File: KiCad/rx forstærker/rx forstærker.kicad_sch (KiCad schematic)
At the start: 11 parts, among them U1 MCP6002-xMC

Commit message: Rx forstærker uden kond
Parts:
- removed C_elektrolyt: 10uF, symbol Device:C
- removed C_evt_elekt+keram: C_Find_værdi, symbol Device:C
- removed C_keramisk: 100nF, symbol Device:C
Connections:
- net VS: now also R1,3.2, U1.3 (+)
- net at R1,1.1, R1,2.1, R1,3.1: now also R3.1, R4.2
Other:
- moved on the sheet: R3, R4

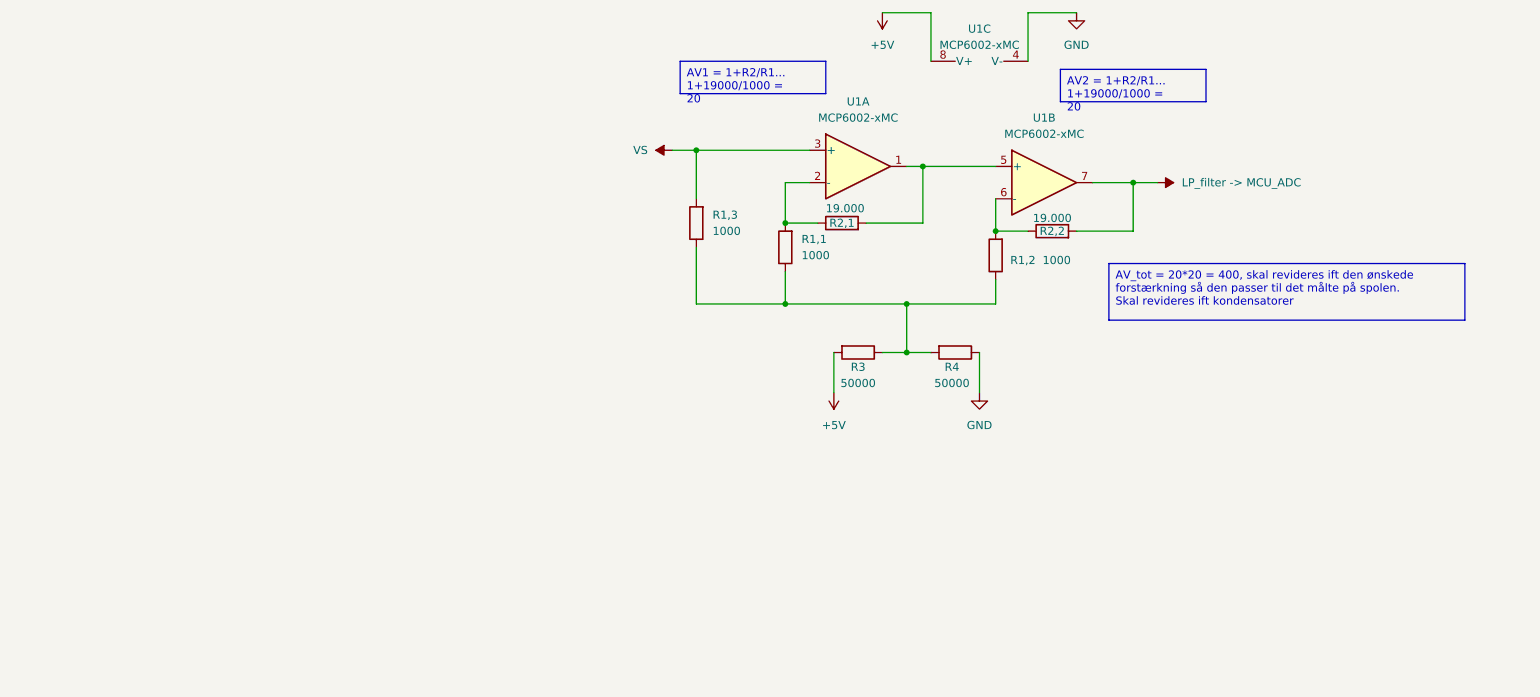
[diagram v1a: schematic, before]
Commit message: RX forstærker + MCU i kicad,mangler footprints2
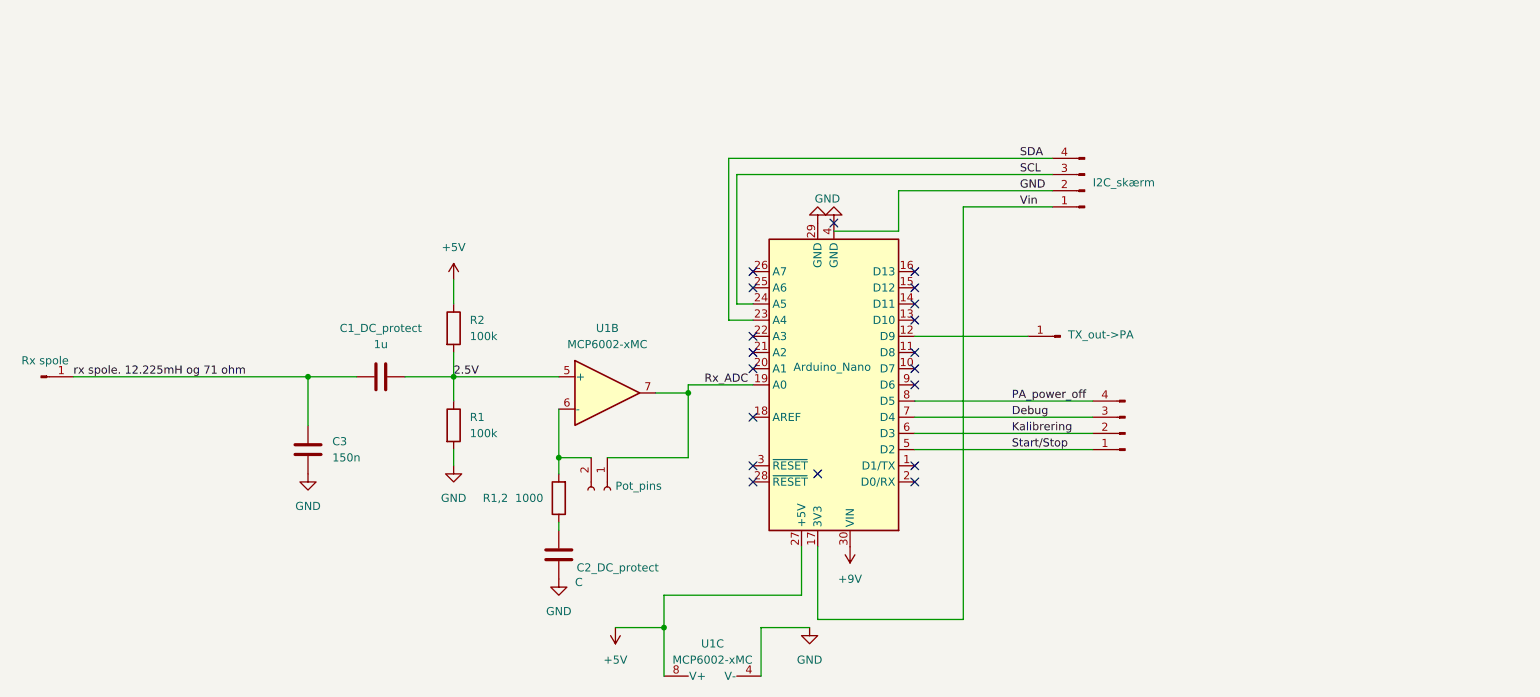
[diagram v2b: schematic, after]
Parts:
- removed R1,1, R1,3: 1000, symbol Device:R
- removed R2,1, R2,2: 19.000, symbol Device:R
- removed R3, R4: 50000, symbol Device:R
- removed unit 1 of U1
- added A1: Arduino_Nano, Module:Arduino_Nano, symbol MCU_Module:Arduino_Nano_v3.x
- added C1_DC_protect: 1u, symbol Device:C
- added C2_DC_protect: C, symbol Device:C
- added C3: 150n, symbol Device:C
- added I2C_skærm, J4: Conn_01x04_Pin, symbol Connector:Conn_01x04_Pin
- added J1: Rx spole, symbol Connector:Conn_01x01_Pin
- added J2: Pot_pins, symbol Connector:Conn_01x02_Socket
- added J3: TX_out->PA, symbol Connector:Conn_01x01_Pin
- added R1, R2: 100k, symbol Device:R
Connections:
- net +5V: now also A1.27 (+5V), R2.1
- net GND: now also A1.29 (GND), A1.4 (GND), C2_DC_protect.1, C3.2, I2C_skærm.2 (Pin_2), R1.2
- net 2.5V: now reaches U1.5 (+)
- net 2.5V: now also C1_DC_protect.2, R1.1, R2.2
- net at R1,2.1: now also C2_DC_protect.2
- net at R1,2.2, U1.6 (-): now also J2.2 (Pin_2)
- net LP_filter -> MCU_ADC renamed Rx_ADC 
- net Rx_ADC : now also A1.19 (A0), J2.1 (Pin_1)
- new net: A1.12 (D9), J3.1 (Pin_1)
- new net +9V: A1.30 (VIN)
- new net Debug: A1.7 (D4), J4.3 (Pin_3)
- new net Kalibrering: A1.6 (D3), J4.2 (Pin_2)
- new net PA_power_off: A1.8 (D5), J4.4 (Pin_4)
- new net SCL: A1.24 (A5), I2C_skærm.3 (Pin_3)
- new net SDA: A1.23 (A4), I2C_skærm.4 (Pin_4)
- new net Start/Stop: A1.5 (D2), J4.1 (Pin_1)
- new net Vin: A1.17 (3V3), I2C_skærm.1 (Pin_1)
- new net rx spole. 12.225mH og 71 ohm: C1_DC_protect.1, C3.1, J1.1 (Pin_1)
- no-connect marks 0 -> 19
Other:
- moved on the sheet: R1,2, U1B, U1C

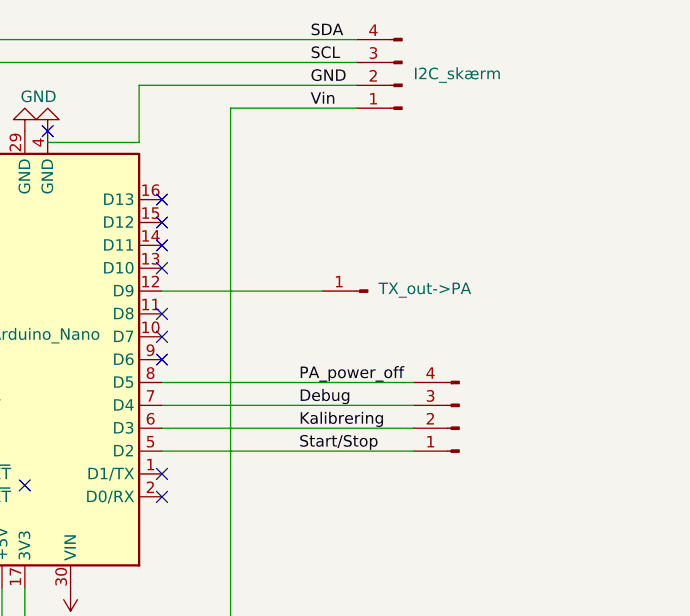
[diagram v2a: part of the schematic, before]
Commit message: rxforstærker simplificeret
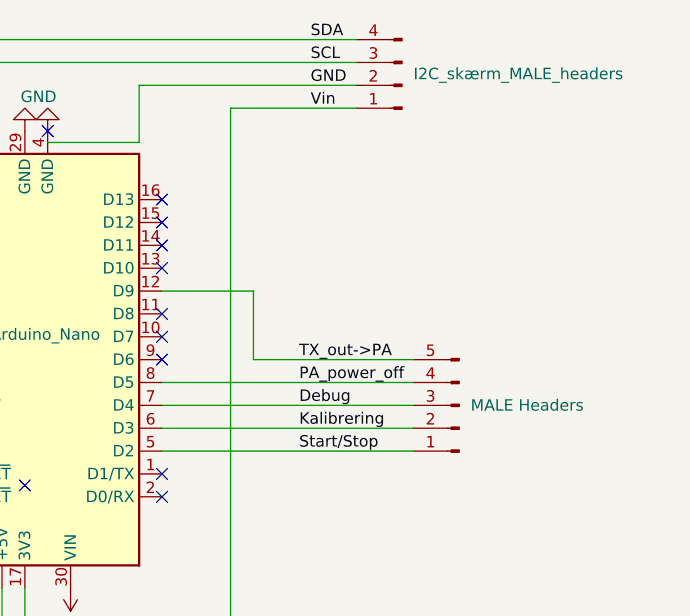
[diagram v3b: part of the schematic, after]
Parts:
- removed J3: TX_out->PA, symbol Connector:Conn_01x01_Pin
- removed J4: Conn_01x04_Pin, symbol Connector:Conn_01x04_Pin
- added J4: MALE Headers, symbol Connector:Conn_01x05_Pin
- renumbered I2C_skærm to I2C_skærm_MALE_headers
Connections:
- net Debug: now also J4.3 (Pin_3)
- net Kalibrering: now also J4.2 (Pin_2)
- net PA_power_off: now also J4.4 (Pin_4)
- net Start/Stop: now also J4.1 (Pin_1)
- net TX_out->PA: now reaches A1.12 (D9)
- net TX_out->PA: now also J4.5 (Pin_5)
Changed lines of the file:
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@@
 	(wire
 		(pts
+			(xy 186.69 92.71) (xy 186.69 100.33)
+		)
+		(stroke
+			(width 0)
+			(type default)
+		)
+	)
+	(wire
+		(pts
 			(xy 120.65 104.14) (xy 120.65 111.76)
 		)
@@
 	(wire
 		(pts
+			(xy 186.69 100.33) (xy 204.47 100.33)
+		)
+		(stroke
+			(width 0)
+			(type default)
+		)
+	)
+	(wire
+		(pts
 			(xy 147.32 64.77) (xy 198.12 64.77)
 		)
@@
 	(wire
 		(pts
-			(xy 176.53 92.71) (xy 194.31 92.71)
+			(xy 176.53 92.71) (xy 186.69 92.71)
 		)
 		(stroke
@@
 		)
 	)
+	(label "TX_out->PA"
+		(at 191.77 100.33 0)
+		(fields_autoplaced yes)
+		(effects
+			(font
+				(size 1.27 1.27)
+			)
+			(justify left bottom)
+		)
+	)
 	(label "SCL"
 		(at 193.04 67.31 0)
@@
 	)
 	(symbol
-		(lib_id "Connector:Conn_01x04_Pin")
-		(at 209.55 107.95 180)
+		(lib_id "Device:C")
+		(at 92.71 99.06 90)
 		(unit 1)
 		(exclude_from_sim no)
@@
 		(dnp no)
 		(fields_autoplaced yes)
-		(property "Reference" "J4"
-			(at 210.82 105.4099 0)
+		(property "Reference" "C1_DC_protect"
+			(at 92.71 91.44 90)
 			(effects
 				(font
 					(size 1.27 1.27)
 				)
-				(justify right)
-				(hide yes)
 			)
 		)
-		(property "Value" "Conn_01x04_Pin"
-			(at 210.82 107.9499 0)
+		(property "Value" "1u"
+			(at 92.71 93.98 90)
 			(effects
 				(font
 					(size 1.27 1.27)
 				)
-				(justify right)
-				(hide yes)
 			)
 		)
 		(property "Footprint" ""
-			(at 209.55 107.95 0)
+			(at 96.52 98.0948 0)
 			(effects
 				(font
@@
 		)
 		(property "Datasheet" "~"
-			(at 209.55 107.95 0)
+			(at 92.71 99.06 0)
 			(effects
 				(font
@@
 			)
 		)
-		(property "Description" "Generic connector, single row, 01x04, script generated"
-			(at 209.55 107.95 0)
+		(property "Description" "Unpolarized capacitor"
+			(at 92.71 99.06 0)
 			(effects
 				(font
@@
 		(pin "1"
 		)
-		(pin "3"
-		)
 		(pin "2"
 		)
-		(pin "4"
-		)
 		(instances
 			(project ""
 				(path "/5c43024a-135c-49bd-9b6f-adf795041e03"
-					(reference "J4")
+					(reference "C1_DC_protect")
 					(unit 1)
 				)
@@
 	)
 	(symbol
-		(lib_id "Device:C")
-		(at 92.71 99.06 90)
+		(lib_id "Device:R")
+		(at 120.65 118.11 180)
 		(unit 1)
 		(exclude_from_sim no)
@@
 		(on_board yes)
 		(dnp no)
-		(fields_autoplaced yes)
-		(property "Reference" "C1_DC_protect"
-			(at 92.71 91.44 90)
+		(property "Reference" "R1,2"
+			(at 108.712 118.11 0)
 			(effects
 				(font
 					(size 1.27 1.27)
 				)
+				(justify right)
 			)
 		)
-		(property "Value" "1u"
-			(at 92.71 93.98 90)
+		(property "Value" "1000"
+			(at 113.792 118.11 0)
 			(effects
 				(font
 					(size 1.27 1.27)
 				)
+				(justify right)
 			)
 		)
 		(property "Footprint" ""
-			(at 96.52 98.0948 0)
+			(at 122.428 118.11 90)
 			(effects
 				(font
@@
 		)
 		(property "Datasheet" "~"
-			(at 92.71 99.06 0)
+			(at 120.65 118.11 0)
 			(effects
 				(font
@@
 			)
 		)
-		(property "Description" "Unpolarized capacitor"
-			(at 92.71 99.06 0)
+		(property "Description" "Resistor"
+			(at 120.65 118.11 0)
 			(effects
 				(font
@@
 		)
 		(instances
-			(project ""
+			(project "Forstærker og LP-filter til metaldetektor"
 				(path "/5c43024a-135c-49bd-9b6f-adf795041e03"
-					(reference "C1_DC_protect")
+					(reference "R1,2")
 					(unit 1)
 				)
@@
 	(symbol
 		(lib_id "Device:R")
-		(at 120.65 118.11 180)
+		(at 104.14 106.68 0)
 		(unit 1)
 		(exclude_from_sim no)
@@
 		(on_board yes)
 		(dnp no)
-		(property "Reference" "R1,2"
-			(at 108.712 118.11 0)
+		(fields_autoplaced yes)
+		(property "Reference" "R1"
+			(at 106.68 105.4099 0)
 			(effects
 				(font
 					(size 1.27 1.27)
 				)
-				(justify right)
+				(justify left)
 			)
 		)
-		(property "Value" "1000"
-			(at 113.792 118.11 0)
+		(property "Value" "100k"
+			(at 106.68 107.9499 0)
 			(effects
 				(font
 					(size 1.27 1.27)
 				)
-				(justify right)
+				(justify left)
 			)
 		)
 		(property "Footprint" ""
-			(at 122.428 118.11 90)
+			(at 102.362 106.68 90)
 			(effects
 				(font
@@
 		)
 		(property "Datasheet" "~"
-			(at 120.65 118.11 0)
+			(at 104.14 106.68 0)
 			(effects
 				(font
@@
 		)
 		(property "Description" "Resistor"
-			(at 120.65 118.11 0)
+			(at 104.14 106.68 0)
 			(effects
 				(font
@@
 			)
 		)
-		(pin "1"
-		)
 		(pin "2"
 		)
+		(pin "1"
+		)
 		(instances
-			(project "Forstærker og LP-filter til metaldetektor"
+			(project ""
 				(path "/5c43024a-135c-49bd-9b6f-adf795041e03"
-					(reference "R1,2")
+					(reference "R1")
 					(unit 1)
 				)
@@
 	)
 	(symbol
-		(lib_id "Device:R")
-		(at 104.14 106.68 0)
+		(lib_id "Connector:Conn_01x05_Pin")
+		(at 209.55 105.41 180)
 		(unit 1)
 		(exclude_from_sim no)
@@
 		(on_board yes)
 		(dnp no)
-		(fields_autoplaced yes)
-		(property "Reference" "R1"
-			(at 106.68 105.4099 0)
+		(property "Reference" "J4"
+			(at 210.82 104.1399 0)
 			(effects
 				(font
 					(size 1.27 1.27)
 				)
-				(justify left)
+				(justify right)
+				(hide yes)
 			)
 		)
-		(property "Value" "100k"
-			(at 106.68 107.9499 0)
+		(property "Value" "MALE Headers"
+			(at 210.82 105.41 0)
 			(effects
 				(font
 					(size 1.27 1.27)
 				)
-				(justify left)
+				(justify right)
 			)
 		)
 		(property "Footprint" ""
-			(at 102.362 106.68 90)
+			(at 209.55 105.41 0)
 			(effects
 				(font
@@
 		)
 		(property "Datasheet" "~"
-			(at 104.14 106.68 0)
+			(at 209.55 105.41 0)
 			(effects
 				(font
@@
 			)
 		)
-		(property "Description" "Resistor"
-			(at 104.14 106.68 0)
+		(property "Description" "Generic connector, single row, 01x05, script generated"
+			(at 209.55 105.41 0)
 			(effects
 				(font
@@
 			)
 		)
+		(pin "1"
+		)
+		(pin "5"
+		)
+		(pin "4"
+		)
 		(pin "2"
 		)
-		(pin "1"
+		(pin "3"
 		)
 		(instances
 			(project ""
 				(path "/5c43024a-135c-49bd-9b6f-adf795041e03"
-					(reference "R1")
+					(reference "J4")
 					(unit 1)
 				)
@@
 		(dnp no)
 		(fields_autoplaced yes)
-		(property "Reference" "I2C_skærm"
+		(property "Reference" "I2C_skærm_MALE_headers"
 			(at 204.47 68.5799 0)
 			(effects
@@
 			(project ""
 				(path "/5c43024a-135c-49bd-9b6f-adf795041e03"
-					(reference "I2C_skærm")
+					(reference "I2C_skærm_MALE_headers")
 					(unit 1)
 				)
@@
 					(unit 1)
 				)
-			)
-		)
-	)
-	(symbol
-		(lib_id "Connector:Conn_01x01_Pin")
-		(at 199.39 92.71 180)
-		(unit 1)
-		(exclude_from_sim no)
-		(in_bom yes)
-		(on_board yes)
-		(dnp no)
-		(property "Reference" "J3"
-			(at 198.755 87.63 0)
-			(effects
-				(font
-					(size 1.27 1.27)
-				)
-				(hide yes)
-			)
-		)
-		(property "Value" "TX_out->PA"
-			(at 205.74 92.456 0)
-			(effects
-				(font
-					(size 1.27 1.27)
-				)
-			)
-		)
-		(property "Footprint" ""
-			(at 199.39 92.71 0)
-			(effects
-				(font
-					(size 1.27 1.27)
-				)
-				(hide yes)
-			)
-		)
-		(property "Datasheet" "~"
-			(at 199.39 92.71 0)
-			(effects
-				(font
-					(size 1.27 1.27)
-				)
-				(hide yes)
-			)
-		)
-		(property "Description" "Generic connector, single row, 01x01, script generated"
-			(at 199.39 92.71 0)
-			(effects
-				(font
-					(size 1.27 1.27)
-				)
-				(hide yes)
-			)
-		)
-		(pin "1"
-		)
-		(instances
-			(project ""
-				(path "/5c43024a-135c-49bd-9b6f-adf795041e03"
-					(reference "J3")
-					(unit 1)
-				)
